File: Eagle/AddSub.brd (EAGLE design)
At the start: 100 x 80 mm, 238 parts, among them Q1 310mA/60V/1.6Ω, Q10 310mA/60V/1.6Ω, Q100 310mA/60V/1.6Ω, Q101 310mA/60V/1.6Ω, Q102 310mA/60V/1.6Ω, Q103 310mA/60V/1.6Ω, Q104 310mA/60V/1.6Ω, Q105 310mA/60V/1.6Ω, Q106 310mA/60V/1.6Ω, Q107 310mA/60V/1.6Ω, Q108 310mA/60V/1.6Ω, Q109 310mA/60V/1.6Ω, Q11 310mA/60V/1.6Ω, Q110 310mA/60V/1.6Ω, Q111 310mA/60V/1.6Ω, Q112 310mA/60V/1.6Ω, Q113 310mA/60V/1.6Ω, Q114 310mA/60V/1.6Ω, Q115 310mA/60V/1.6Ω, Q116 310mA/60V/1.6Ω, Q117 310mA/60V/1.6Ω, Q118 310mA/60V/1.6Ω, Q119 310mA/60V/1.6Ω, Q12 310mA/60V/1.6Ω, Q120 310mA/60V/1.6Ω, Q121 310mA/60V/1.6Ω, Q122 310mA/60V/1.6Ω, Q123 310mA/60V/1.6Ω, Q124 310mA/60V/1.6Ω, Q125 310mA/60V/1.6Ω, Q126 310mA/60V/1.6Ω, Q127 310mA/60V/1.6Ω, Q13 310mA/60V/1.6Ω, Q134 310mA/60V/1.6Ω, Q135 310mA/60V/1.6Ω, Q136 310mA/60V/1.6Ω, Q137 310mA/60V/1.6Ω, Q138 310mA/60V/1.6Ω, Q139 310mA/60V/1.6Ω, Q14 310mA/60V/1.6Ω, Q140 310mA/60V/1.6Ω, Q148 310mA/60V/1.6Ω, Q149 310mA/60V/1.6Ω, Q15 310mA/60V/1.6Ω, Q150 310mA/60V/1.6Ω, Q151 310mA/60V/1.6Ω, Q152 310mA/60V/1.6Ω, Q153 310mA/60V/1.6Ω, Q154 310mA/60V/1.6Ω, Q16 310mA/60V/1.6Ω, Q162 310mA/60V/1.6Ω, Q163 310mA/60V/1.6Ω, Q164 310mA/60V/1.6Ω, Q165 310mA/60V/1.6Ω, Q166 310mA/60V/1.6Ω, Q167 310mA/60V/1.6Ω, Q168 310mA/60V/1.6Ω, Q17 310mA/60V/1.6Ω, Q176 310mA/60V/1.6Ω, Q177 310mA/60V/1.6Ω, Q178 310mA/60V/1.6Ω, Q179 310mA/60V/1.6Ω, Q18 310mA/60V/1.6Ω, Q180 310mA/60V/1.6Ω, Q181 310mA/60V/1.6Ω, Q182 310mA/60V/1.6Ω, Q19 310mA/60V/1.6Ω, Q2 310mA/60V/1.6Ω, Q20 310mA/60V/1.6Ω, Q21 310mA/60V/1.6Ω, Q22 310mA/60V/1.6Ω, Q23 310mA/60V/1.6Ω, Q24 310mA/60V/1.6Ω, Q25 310mA/60V/1.6Ω, Q26 310mA/60V/1.6Ω, Q27 310mA/60V/1.6Ω, Q28 310mA/60V/1.6Ω, Q29 310mA/60V/1.6Ω, Q3 310mA/60V/1.6Ω, Q30 310mA/60V/1.6Ω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

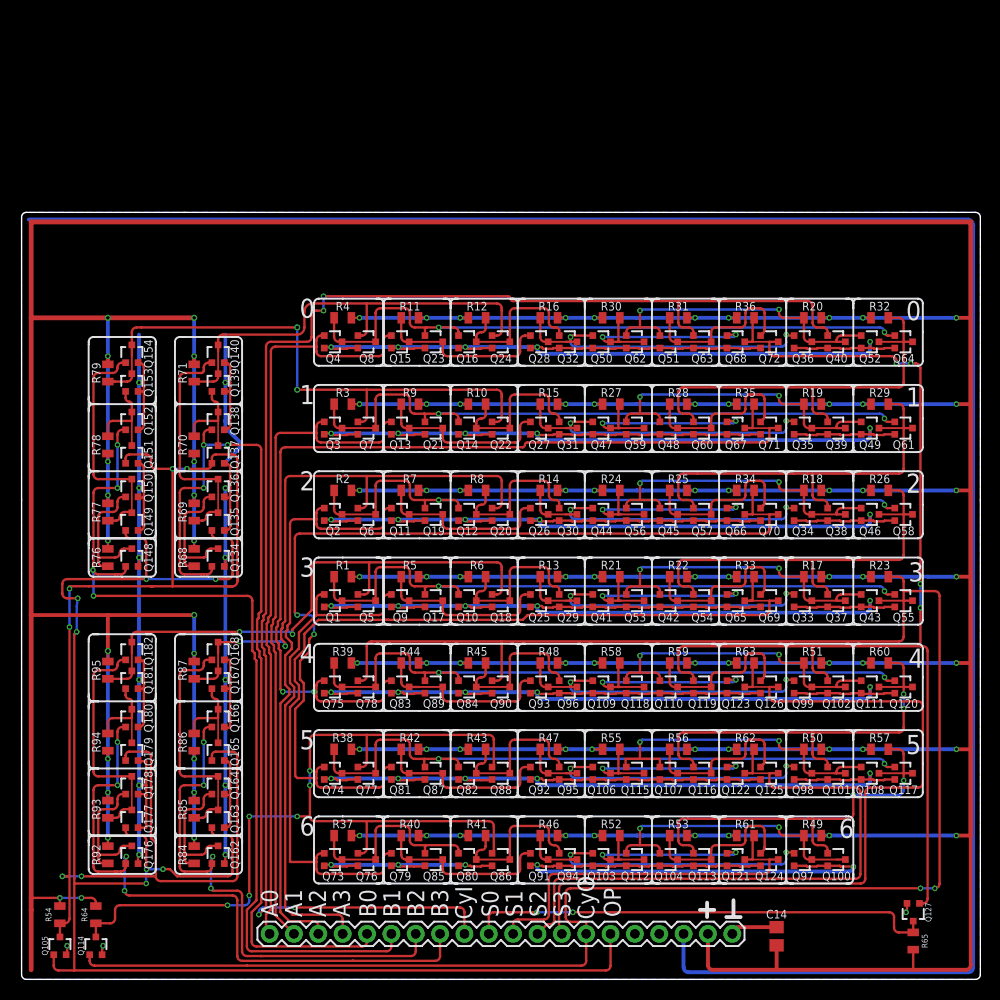
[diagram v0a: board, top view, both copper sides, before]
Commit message: Rerouted for SOT23
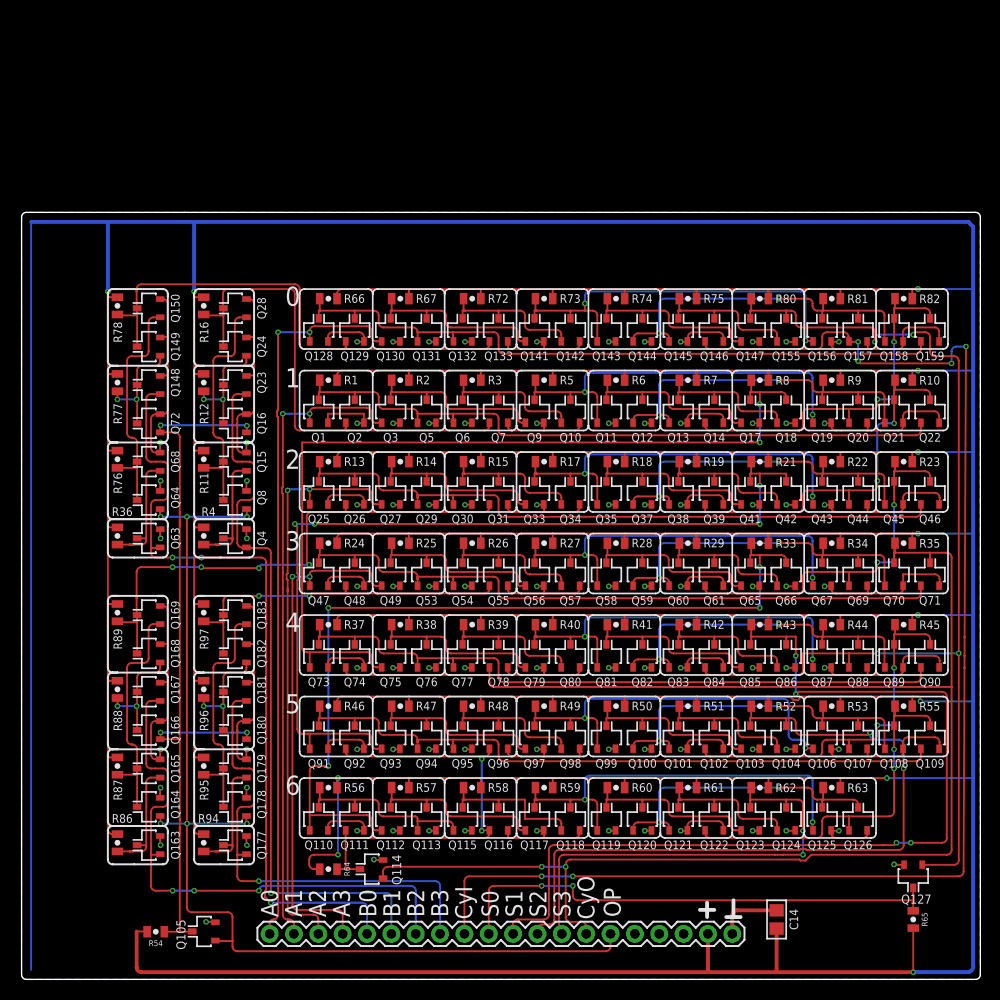
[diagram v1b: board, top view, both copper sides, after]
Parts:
- removed Q134, Q135, Q136, Q137, Q138, Q139, Q140, Q151, Q152, Q153, Q154, Q162, Q176, Q32, Q36, Q40, Q50, Q51, Q52, Q62: 310mA/60V/1.6Ω, SparkFun-DiscreteSemi:SOT323
- removed R20, R30, R31, R32, R68, R69, R70, R71, R79, R84, R85, R92, R93: (no value), SparkFun-Resistors:0805
- added Q128, Q129, Q130, Q131, Q132, Q133, Q141, Q142, Q143, Q144, Q145, Q146, Q147, Q155, Q156, Q157, Q158, Q159, Q169, Q183: 310mA/60V/1.6Ω, XSNOR:SOT23
- added R66, R67, R72, R73, R74, R75, R80, R81, R82, R88, R89, R96, R97: (no value), XSNOR:0805
- Q1, Q10, Q100, Q101, Q102, Q103, Q104, Q105, Q106, Q107, Q108, Q109, Q11, Q110, Q111, Q112, Q113, Q114, Q115, Q116, Q117, Q118, Q119, Q12, Q120, Q121, Q122, Q123, Q124, Q125, Q126, Q127, Q13, Q14, Q148, Q149, Q15, Q150, Q16, Q163, Q164, Q165, Q166, Q167, Q168, Q17, Q177, Q178, Q179, Q18, Q180, Q181, Q182, Q19, Q2, Q20, Q21, Q22, Q23, Q24, Q25, Q26, Q27, Q28, Q29, Q3, Q30, Q31, Q33, Q34, Q35, Q37, Q38, Q39, Q4, Q41, Q42, Q43, Q44, Q45, Q46, Q47, Q48, Q49, Q5, Q53, Q54, Q55, Q56, Q57, Q58, Q59, Q6, Q60, Q61, Q63, Q64, Q65, Q66, Q67, Q68, Q69, Q7, Q70, Q71, Q72, Q73, Q74, Q75, Q76, Q77, Q78, Q79, Q8, Q80, Q81, Q82, Q83, Q84, Q85, Q86, Q87, Q88, Q89, Q9, Q90, Q91, Q92, Q93, Q94, Q95, Q96, Q97, Q98, Q99: device SparkFun-DiscreteSemi:SOT323 -> XSNOR:SOT23
- R1, R10, R11, R12, R13, R14, R15, R16, R17, R18, R19, R2, R21, R22, R23, R24, R25, R26, R27, R28, R29, R3, R33, R34, R35, R36, R37, R38, R39, R4, R40, R41, R42, R43, R44, R45, R46, R47, R48, R49, R5, R50, R51, R52, R53, R54, R55, R56, R57, R58, R59, R6, R60, R61, R62, R63, R64, R65, R7, R76, R77, R78, R8, R86, R87, R9, R94, R95: device SparkFun-Resistors:0805 -> XSNOR:0805
- moved Q64 80.5 mm to (13.2, 50.0), turned to 90 degrees
- moved R36 69.3 mm to (10.0, 46.2), turned to 90 degrees
- moved Q72 65.3 mm to (13.2, 58.0), turned to 90 degrees
- moved Q68 62.5 mm to (13.2, 54.0), turned to 90 degrees
- moved Q63 61.3 mm to (13.2, 46.0), turned to 90 degrees
- moved Q111 55.5 mm to (34.8, 16.8), turned to 0 degrees
- moved Q49 52.3 mm to (38.5, 42.2), turned to 0 degrees
- moved R57 50.2 mm to (39.5, 20.0), turned to 0 degrees
- moved Q89 48.1 mm to (91.0, 33.8), turned to 0 degrees
- moved Q21 48.0 mm to (91.0, 59.2), turned to 0 degrees
- moved Q90 44.9 mm to (94.8, 33.8), turned to 0 degrees
- moved Q22 44.8 mm to (94.8, 59.2), turned to 0 degrees
- moved R45 44.7 mm to (92.0, 37.0), turned to 0 degrees
- moved R10 44.6 mm to (92.0, 62.5), turned to 0 degrees
- moved R44 44.2 mm to (84.5, 37.0)
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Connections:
- removed net N$1: Q134.3, Q136.1, R68.1
- removed net N$2: Q73.3, Q76.3, Q80.1, Q85.1, R37.1
- removed net N$4: Q148.3, Q150.1, R76.1
- removed net N1: Q137.3, Q138.3, Q139.1, R70.1
- removed net N10: Q28.3, Q32.3, Q36.1, Q50.1, R16.1
- removed net N11: Q51.3, Q63.3, Q72.1, R31.1
- removed net N13: Q36.3, Q40.3, Q51.1, Q52.1, Q62.1, R20.1
- removed net N14: Q16.1, Q23.1, Q4.3, Q64.1, Q8.3, R4.1
- removed net N18: Q165.3, Q166.3, Q167.1, R86.1
- removed net N19: Q163.3, Q164.3, Q168.1, R85.1
- removed net N2: Q135.3, Q136.3, Q140.1, R69.1
- removed net N22: Q14.3, Q22.3, Q31.1, R10.1
- removed net N23: Q13.3, Q21.3, Q27.1, R9.1
- removed net N24: Q27.3, Q31.3, Q35.1, Q47.1, R15.1
- removed net N25: Q48.3, Q60.3, Q71.1, R28.1
- removed net N26: Q47.3, Q59.3, Q67.1, R27.1
- removed net N27: Q35.3, Q39.3, Q48.1, Q49.1, Q59.1, R19.1
- removed net N28: Q14.1, Q21.1, Q3.3, Q61.1, Q7.3, R3.1
- removed net N29: Q179.3, Q180.3, Q181.1, R94.1
- removed net N30: Q177.3, Q178.3, Q182.1, R93.1
- removed net N36: Q12.3, Q20.3, Q30.1, R8.1
- removed net N37: Q11.3, Q19.3, Q26.1, R7.1
- removed net N38: Q26.3, Q30.3, Q34.1, Q44.1, R14.1
- removed net N39: Q45.3, Q57.3, Q70.1, R25.1
- removed net N40: Q44.3, Q56.3, Q66.1, R24.1
- removed net N41: Q34.3, Q38.3, Q45.1, Q46.1, Q56.1, R18.1
- removed net N42: Q12.1, Q19.1, Q2.3, Q58.1, Q6.3, R2.1
- removed net N5: Q151.3, Q152.3, Q153.1, R78.1
- removed net N50: Q10.3, Q18.3, Q29.1, R6.1
- removed net N51: Q17.3, Q25.1, Q9.3, R5.1
- removed net N52: Q25.3, Q29.3, Q33.1, Q41.1, R13.1
- removed net N53: Q42.3, Q54.3, Q69.1, R22.1
- removed net N54: Q41.3, Q53.3, Q65.1, R21.1
- removed net N55: Q33.3, Q37.3, Q42.1, Q43.1, Q53.1, R17.1
- removed net N56: Q1.3, Q10.1, Q17.1, Q5.3, Q55.1, R1.1
- removed net N6: Q149.3, Q150.3, Q154.1, R77.1
- removed net N64: Q84.3, Q90.3, Q96.1, R45.1
- removed net N65: Q83.3, Q89.3, Q93.1, R44.1
- removed net N66: Q109.1, Q93.3, Q96.3, Q99.1, R48.1
- removed net N67: Q110.3, Q119.3, Q126.1, R59.1
- removed net N68: Q109.3, Q118.3, Q123.1, R58.1
- removed net N69: Q102.3, Q110.1, Q111.1, Q118.1, Q99.3, R51.1
- removed net N70: Q120.1, Q75.3, Q78.3, Q84.1, Q89.1, R39.1
- removed net N78: Q82.3, Q88.3, Q95.1, R43.1
- removed net N79: Q81.3, Q87.3, Q92.1, R42.1
- removed net N8: Q16.3, Q24.3, Q32.1, R12.1
- removed net N80: Q106.1, Q92.3, Q95.3, Q98.1, R47.1
- removed net N81: Q107.3, Q116.3, Q125.1, R56.1
- removed net N82: Q106.3, Q115.3, Q122.1, R55.1
- removed net N83: Q101.3, Q107.1, Q108.1, Q115.1, Q98.3, R50.1
- removed net N84: Q117.1, Q74.3, Q77.3, Q82.1, Q87.1, R38.1
- removed net N9: Q15.3, Q23.3, Q28.1, R11.1
- removed net N92: Q80.3, Q86.3, Q94.1, R41.1
- removed net N93: Q79.3, Q85.3, Q91.1, R40.1
- removed net N94: Q103.1, Q91.3, Q94.3, Q97.1, R46.1
- removed net N95: Q104.3, Q113.3, Q124.1, R53.1
- removed net N96: Q103.3, Q112.3, Q121.1, R52.1
- removed net N97: Q100.3, Q104.1, Q112.1, Q97.3, R49.1
- new net N$10: Q12.1, Q13.1, Q19.3, Q20.3, Q21.1, R9.1
- new net N$101: Q128.3, Q129.3, Q131.1, Q132.1, Q159.1, R66.1
- new net N$1016: Q37.1, Q38.1, Q43.3, Q44.3, Q45.1, R22.1
- new net N$1017: Q25.3, Q26.3, Q29.1, Q30.1, Q46.1, R13.1
- new net N$102: Q132.3, Q133.3, Q142.1, R72.1
- new net N$104: Q141.3, Q142.3, Q143.1, Q156.1, R73.1
- new net N$106: Q145.3, Q146.3, Q155.1, R75.1
- new net N$108: Q143.3, Q144.3, Q147.1, R74.1
- new net N$11: Q10.3, Q11.1, Q19.1, Q9.3, R5.1
- new net N$12: Q10.1, Q6.3, Q7.3, R3.1
- new net N$124: Q73.3, Q74.3, Q76.1, Q77.1, Q90.1, R37.1
- new net N$1257: Q109.1, Q91.3, Q92.3, Q94.1, Q95.1, R46.1
- new net N$13: Q3.3, Q5.3, Q9.1, R2.1
- new net N$14: Q11.3, Q12.3, Q17.1, R6.1
- new net N$15: Q13.3, Q14.3, Q18.1, R7.1
- new net N$152: Q110.3, Q111.3, Q113.1, Q115.1, R56.1
- new net N$18: Q38.3, Q39.3, Q42.1, R19.1
- new net N$19: Q33.3, Q34.3, Q35.1, Q43.1, R17.1
- new net N$20: Q30.3, Q31.3, Q34.1, R15.1
- new net N$21: Q27.3, Q29.3, Q33.1, R14.1
- new net N$22: Q47.3, Q48.3, Q53.1, Q54.1, Q71.1, R24.1
- new net N$224: Q77.3, Q78.3, Q80.1, R39.1
- new net N$23: Q56.3, Q57.3, Q58.1, Q67.1, R27.1
- new net N$24: Q54.3, Q55.3, Q57.1, R26.1
- new net N$25: Q49.3, Q53.3, Q56.1, R25.1
- new net N$26: Q59.1, Q60.1, Q67.3, Q69.3, Q70.1, R34.1
- new net N$27: Q60.3, Q61.3, Q66.1, R29.1
- new net N$28: Q58.3, Q59.3, Q65.1, R28.1
- new net N$293: Q95.3, Q96.3, Q98.1, R48.1
- new net N$298: Q115.3, Q116.3, Q118.1, R58.1
- new net N$3: Q112.3, Q113.3, Q117.1, R57.1
- new net N$32: Q63.3, Q68.1, R36.1
- new net N$324: Q75.3, Q76.3, Q79.1, R38.1
- new net N$33: Q150.1, Q64.3, Q68.3, R76.1
- new net N$34: Q148.3, Q149.1, Q72.3, R77.1
- new net N$344: Q93.3, Q94.3, Q97.1, R47.1
- new net N$362: Q83.3, Q84.3, Q86.1, R42.1
- new net N$367: Q130.3, Q131.3, Q141.1, R67.1
- new net N$38: Q163.3, Q165.1, R86.1
- new net N$39: Q164.3, Q165.3, Q169.1, R87.1
- new net N$40: Q166.3, Q167.3, Q168.1, R88.1
- new net N$425: Q79.3, Q80.3, Q81.1, Q87.1, R40.1
- new net N$44: Q106.1, Q97.3, Q98.3, Q99.1, R49.1
- new net N$45: Q177.3, Q179.1, R94.1
- new net N$457: Q120.1, Q121.1, Q125.3, Q126.3, R63.1
- new net N$46: Q178.3, Q179.3, Q183.1, R95.1
- new net N$47: Q180.3, Q181.3, Q182.1, R96.1
- new net N$477: Q117.3, Q118.3, Q119.1, Q125.1, R59.1
- new net N$5: Q144.1, Q145.1, Q156.3, Q157.3, Q158.1, R81.1
- new net N$5234: Q82.1, Q83.1, Q87.3, Q88.3, Q89.1, R44.1
- new net N$55: Q100.1, Q101.1, Q106.3, Q107.3, Q108.1, R53.1
- new net N$615: Q101.3, Q102.3, Q104.1, R51.1
- new net N$627: Q121.3, Q122.3, Q124.1, R61.1
- new net N$7: Q15.3, Q28.1, Q8.3, R11.1
- new net N$713: Q119.3, Q120.3, Q123.1, R60.1
- new net N$715: Q100.3, Q103.1, Q99.3, R50.1
- new net N$768: Q81.3, Q82.3, Q85.1, R41.1
- new net N$9: Q1.3, Q2.3, Q22.1, Q5.1, Q6.1, R1.1
- net /CRYOUT: now also Q111.1, Q116.1, Q92.1, Q96.1; no longer Q76.1, Q77.1, Q86.1, Q88.1
- net /OP: now also Q16.1, Q166.1, Q180.1, Q72.1; no longer Q137.1, Q151.1, Q165.1, Q179.1
- net A0: now also Q128.1, Q130.1; no longer Q15.1, Q4.1
- net A1: now also Q1.1; no longer Q13.1
- net A2: now also Q25.1, Q27.1; no longer Q11.1, Q2.1
- net A3: now also Q47.1, Q49.1; no longer Q1.1, Q9.1
- net B0: now also Q148.1, Q63.1; no longer Q134.1, Q138.1
- net B0': now also Q129.1, Q133.1, Q149.3, Q150.3, R78.1; no longer Q139.3, Q140.3, Q24.1, Q8.1, R71.1
- net B1: now also Q23.1, Q4.1; no longer Q148.1, Q152.1
- net B1': now also Q2.1, Q24.3, Q28.3, R16.1; no longer Q153.3, Q154.3, Q22.1, R79.1
- net B2: now also Q163.1, Q167.1; no longer Q162.1, Q166.1
- net B2': now also Q169.3, Q26.1, Q31.1, R89.1; no longer Q167.3, Q20.1, Q6.1, R87.1
- net B3: now also Q177.1, Q181.1; no longer Q176.1, Q180.1
- net B3': now also Q183.3, Q48.1, Q55.1, R97.1; no longer Q18.1, Q181.3, Q5.1, R95.1
- net C01: now also Q14.1, Q158.3, Q159.3, Q20.1, R82.1; no longer Q39.1, Q52.3, Q60.1, Q64.3, R32.1
- net C12: now also Q21.3, Q22.3, Q39.1, Q44.1, R10.1; no longer Q38.1, Q49.3, Q57.1, Q61.3, R29.1
- net C23: now also Q45.3, Q61.1, Q69.1, R23.1; no longer Q37.1, Q54.1, Q58.3, R26.1
- net C45: now also Q102.1, Q107.1, Q89.3, Q90.3, R45.1; no longer Q101.1, Q111.3, Q116.1, Q120.3, R60.1
- net C56: now also Q109.3, Q122.1, Q126.1, R55.1; no longer Q100.1, Q113.1, Q117.3, R57.1
- net CRYIN: now also Q146.1, Q157.1; no longer Q40.1, Q63.1
- net CRYOUT: now also Q70.3, Q71.3, Q74.1, R35.1; no longer Q43.3, Q55.3, Q90.1, R23.1
- net GND: now also Q128.2, Q129.2, Q130.2, Q131.2, Q132.2, Q133.2, Q141.2, Q142.2, Q143.2, Q144.2, Q145.2, Q146.2, Q147.2, Q155.2, Q156.2, Q157.2, Q158.2, Q159.2, Q169.2, Q183.2; no longer Q134.2, Q135.2, Q136.2, Q137.2, Q138.2, Q139.2, Q140.2, Q151.2, Q152.2, Q153.2, Q154.2, Q162.2, Q176.2, Q32.2, Q36.2, Q40.2, Q50.2, Q51.2, Q52.2, Q62.2
- net N$6: now also Q15.1, Q4.3, R4.1; no longer Q162.3, Q164.1, R84.1
- net N$8: now also Q16.3, Q23.3, Q24.1, R12.1; no longer Q176.3, Q178.1, R92.1
- net N12: now also Q35.3, Q37.3, Q41.1, R18.1; no longer Q50.3, Q62.3, Q68.1, R30.1
- net OP: now also Q164.1, Q178.1, Q64.1, Q8.1; no longer Q135.1, Q149.1, Q163.1, Q177.1
- net SUM0': now also Q147.3, Q155.3, Q84.1, Q88.1, R80.1; no longer Q102.1, Q119.1, Q68.3, Q72.3, R36.1
- net SUM1: now also Q85.3, Q86.3, R43.1; no longer Q121.3, Q124.3, R61.1
- net SUM1': now also Q17.3, Q18.3, Q73.1, R8.1; no longer Q67.3, Q71.3, Q83.1, R35.1
- net SUM2: now also Q103.3, Q104.3, R52.1; no longer Q122.3, Q125.3, R62.1
- net SUM2': now also Q41.3, Q42.3, Q91.1, Q93.1, R21.1; no longer Q66.3, Q70.3, Q74.1, Q81.1, R34.1
- net SUM3: now also Q124.3, R62.1; no longer Q126.3, R63.1
- net SUM3': now also Q110.1, Q112.1, Q66.3; no longer Q69.3, Q73.1, Q79.1
- net VCC: now also R66.2, R67.2, R72.2, R73.2, R74.2, R75.2, R80.2, R81.2, R82.2, R88.2, R89.2, R96.2, R97.2; no longer R20.2, R30.2, R31.2, R32.2, R68.2, R69.2, R70.2, R71.2, R79.2, R84.2, R85.2, R92.2, R93.2
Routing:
- net GND: track 909.5 -> 396.4 mm, vias 50 -> 92
- net LEDPWR: track 210.3 -> 0.00 mm
- net VCC: track 937.5 -> 1044.9 mm, vias 90 -> 12
- net N$124: track 0.00 -> 72.1 mm
- net N$22: track 0.00 -> 71.9 mm
- net N$1257: track 0.00 -> 71.9 mm
- net N$1017: track 0.00 -> 71.9 mm
- net N$101: track 0.00 -> 71.6 mm
- net N$9: track 0.00 -> 71.6 mm
- net N56: track 69.2 -> 0.00 mm, vias 2 -> 0
- net N14: track 69.2 -> 0.00 mm, vias 2 -> 0
- net N84: track 69.2 -> 0.00 mm, vias 2 -> 0
- net N70: track 69.2 -> 0.00 mm, vias 2 -> 0
- net N42: track 69.2 -> 0.00 mm, vias 2 -> 0
- net N28: track 69.2 -> 0.00 mm, vias 2 -> 0
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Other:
- board text added: "Addder/ Subtractor rev 1"
- board text added: "SmallRoomLabs"

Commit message: Centered design on PCB
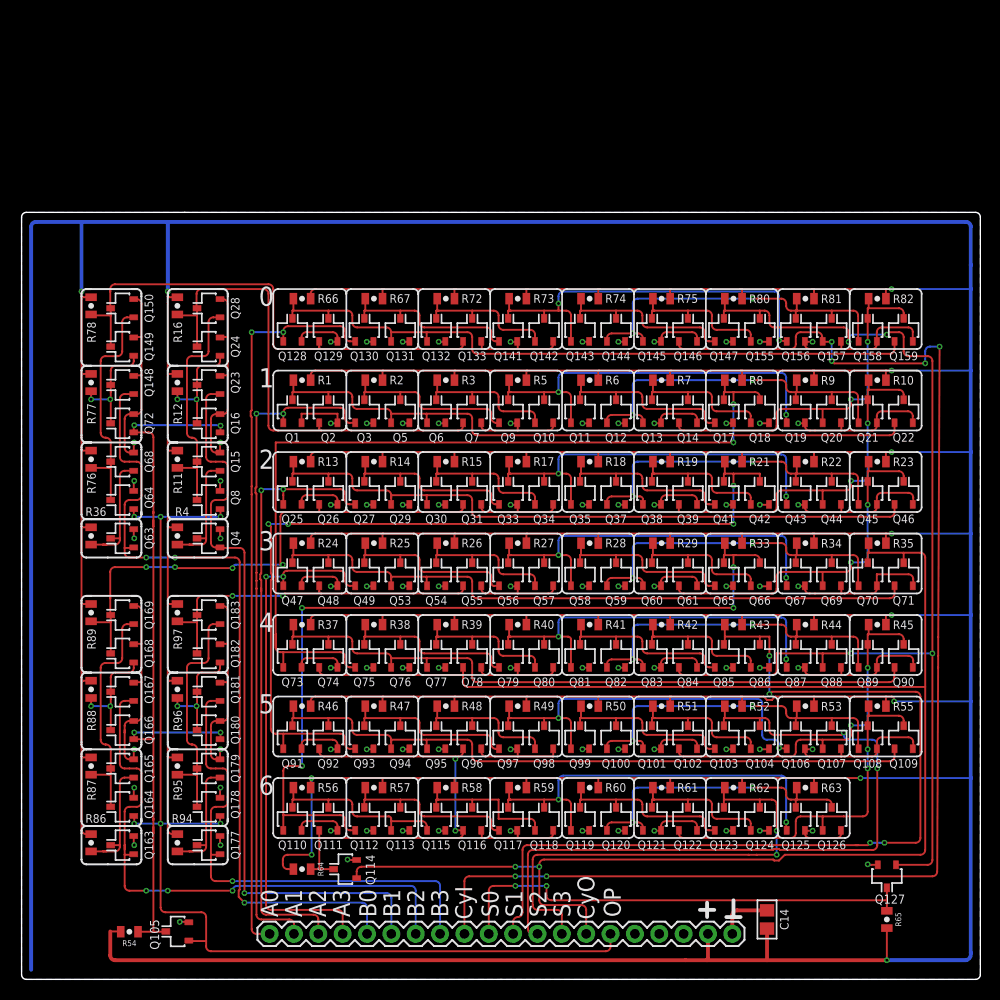
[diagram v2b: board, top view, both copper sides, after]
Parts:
- moved Q1 2.75 mm to (28.2, 59.2)
- moved Q10 2.75 mm to (54.5, 59.2)
- moved Q100 2.75 mm to (62.0, 25.2)
- moved Q101 2.75 mm to (65.8, 25.2)
- moved Q102 2.75 mm to (69.5, 25.2)
- moved Q103 2.75 mm to (73.2, 25.2)
- moved Q104 2.75 mm to (77.0, 25.2)
- moved Q105 2.75 mm to (16.2, 5.00)
- moved Q106 2.75 mm to (80.8, 25.2)
- moved Q107 2.75 mm to (84.5, 25.2)
- moved Q108 2.75 mm to (88.2, 25.2)
- moved Q109 2.75 mm to (92.0, 25.2)
- moved Q11 2.75 mm to (58.2, 59.2)
- moved Q110 2.75 mm to (28.2, 16.8)
- moved Q111 2.75 mm to (32.0, 16.8)
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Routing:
- net VCC: track 1044.9 -> 1058.0 mm
- net CRYOUT: track 175.0 -> 177.8 mm
- net OP: track 113.2 -> 116.0 mm
- net CRYIN: track 145.9 -> 143.2 mm
- net B3: track 49.8 -> 52.6 mm
- net B2: track 57.4 -> 60.2 mm
- net B1: track 75.4 -> 78.2 mm
- net B0: track 82.7 -> 85.5 mm
- net A3: track 53.5 -> 56.3 mm
- net A2: track 61.7 -> 64.5 mm
- net A1: track 67.6 -> 70.3 mm
- net SUM0: track 52.6 -> 49.8 mm
- net SUM1: track 98.7 -> 96.0 mm
- net SUM3: track 47.6 -> 49.9 mm
- net A0: track 76.3 -> 77.5 mm
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
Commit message: Cleanups of PCBs
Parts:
- J1: device SparkFun-Connectors:1X20 -> XSNOR:1X20/90
- moved J1 24.0 mm to (49.9, 4.75)

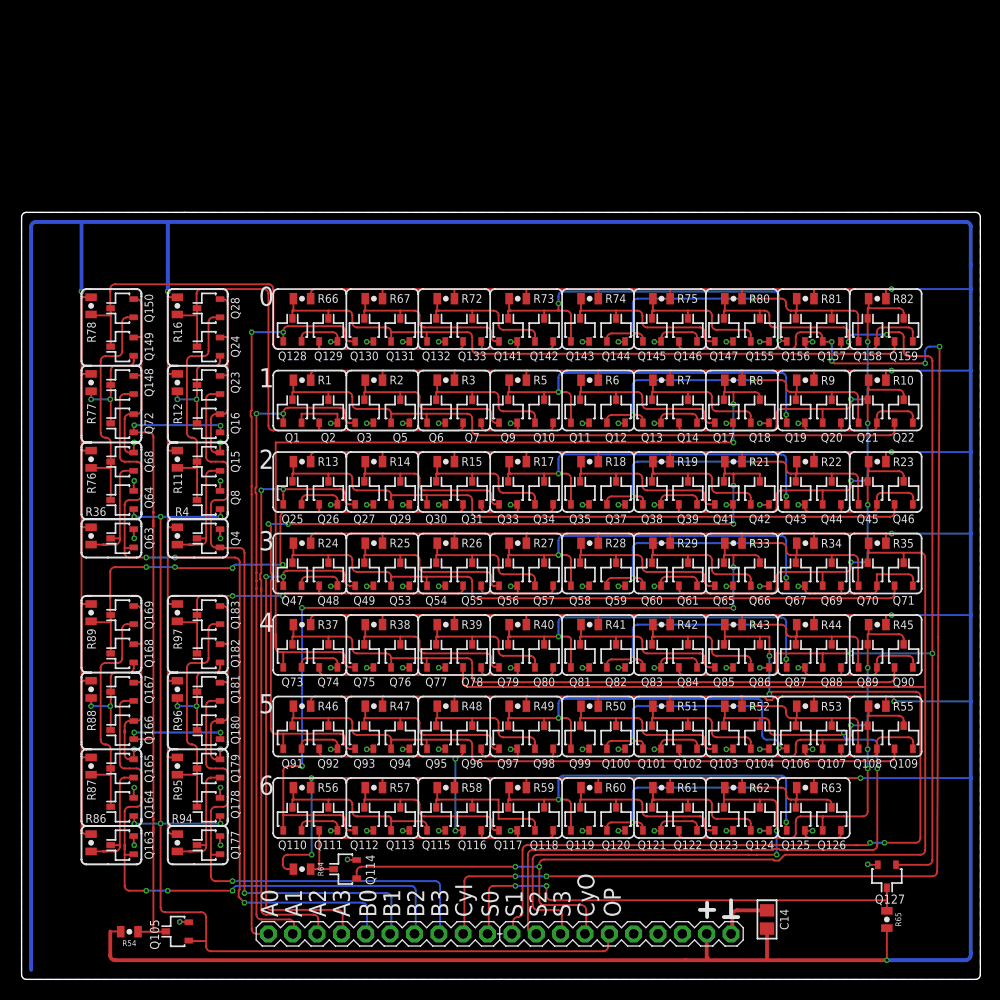
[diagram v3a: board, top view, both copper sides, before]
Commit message: Silk cleanup. Routing of GND instead of floodfill
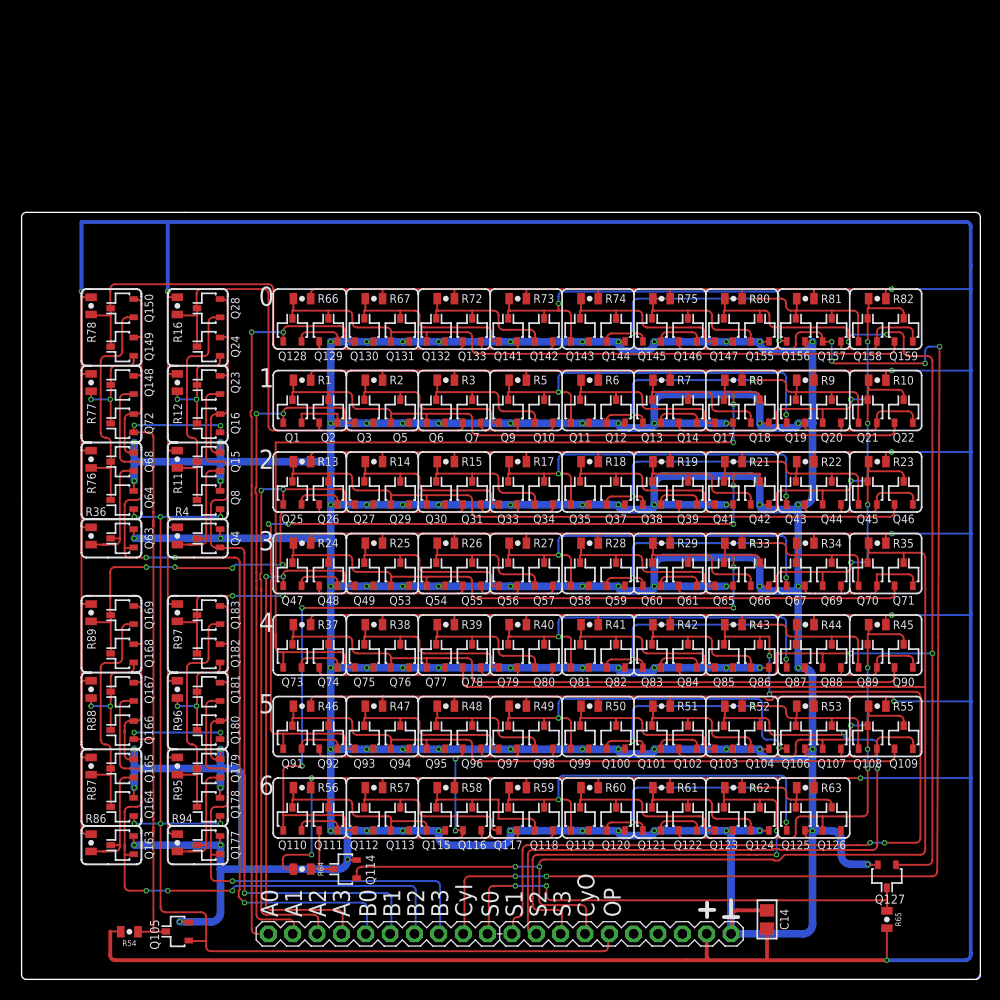
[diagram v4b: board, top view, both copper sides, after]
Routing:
- net GND: track 395.2 -> 1034.8 mm
- net VCC: track 1058.1 -> 975.1 mm

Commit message: Updated boards with pcb template
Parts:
- moved Q128 14.0 mm to (28.2, 81.8)
- moved Q129 14.0 mm to (32.0, 81.8)
- moved Q130 14.0 mm to (35.8, 81.8)
- moved Q131 14.0 mm to (39.5, 81.8)
- moved Q132 14.0 mm to (43.2, 81.8)
- moved Q133 14.0 mm to (47.0, 81.8)
- moved Q141 14.0 mm to (50.8, 81.8)
- moved Q142 14.0 mm to (54.5, 81.8)
- moved Q143 14.0 mm to (58.2, 81.8)
- moved Q144 14.0 mm to (62.0, 81.8)
- moved Q145 14.0 mm to (65.8, 81.8)
- moved Q146 14.0 mm to (69.5, 81.8)
- moved Q147 14.0 mm to (73.2, 81.8)
- moved Q155 14.0 mm to (77.0, 81.8)
- moved Q156 14.0 mm to (80.8, 81.8)
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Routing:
- net VCC: track 975.1 -> 1066.3 mm, vias 12 -> 14
- net GND: track 1034.8 -> 1079.8 mm
- net OP: track 115.8 -> 134.8 mm
- net SUM0': track 116.3 -> 129.9 mm
- net CRYIN: track 143.2 -> 156.8 mm
- net A0: track 77.4 -> 90.6 mm
- net A1: track 70.4 -> 83.4 mm
- net A2: track 64.6 -> 76.6 mm
- net B0: track 85.5 -> 97.4 mm
- net B1: track 78.3 -> 89.6 mm
- net A3: track 56.4 -> 67.4 mm
- net B3: track 52.6 -> 63.5 mm
- net B2: track 60.2 -> 69.4 mm
- net SUM1: track 96.1 -> 105.2 mm
- net SUM2: track 77.3 -> 85.6 mm
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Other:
- board size 100 x 80 mm -> 100 x 100 mm
- board text added: "Adder/ subtractor rev1"
- board text removed: "Addder/ Subtractor rev 1"
